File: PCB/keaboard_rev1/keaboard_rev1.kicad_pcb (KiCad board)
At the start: 2 copper layers, 141.9 x 93.7 mm, 61 parts, among them K01 KEYSW, K02 KEYSW, K03 KEYSW, K04 KEYSW, K05 KEYSW, K06 KEYSW, K07 KEYSW, K08 KEYSW, K09 KEYSW, K10 KEYSW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

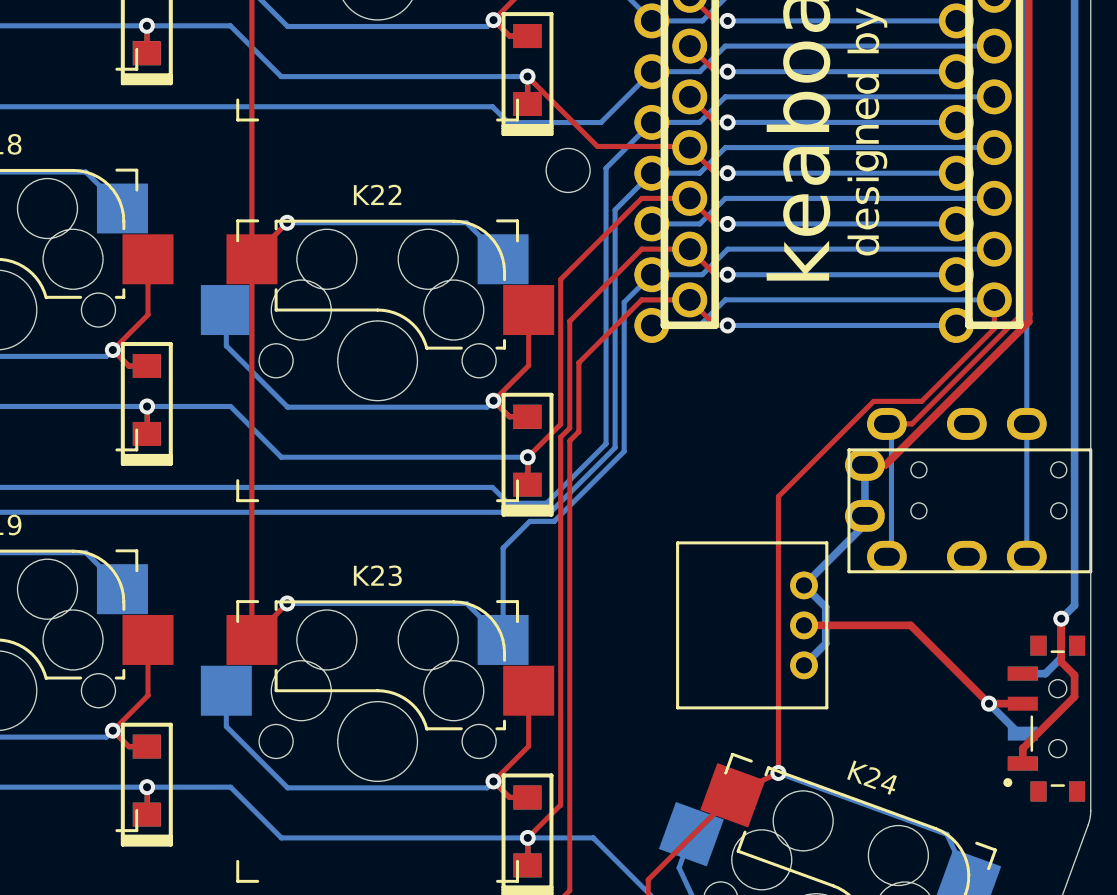
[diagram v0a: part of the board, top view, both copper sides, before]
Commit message: Fix missing trace
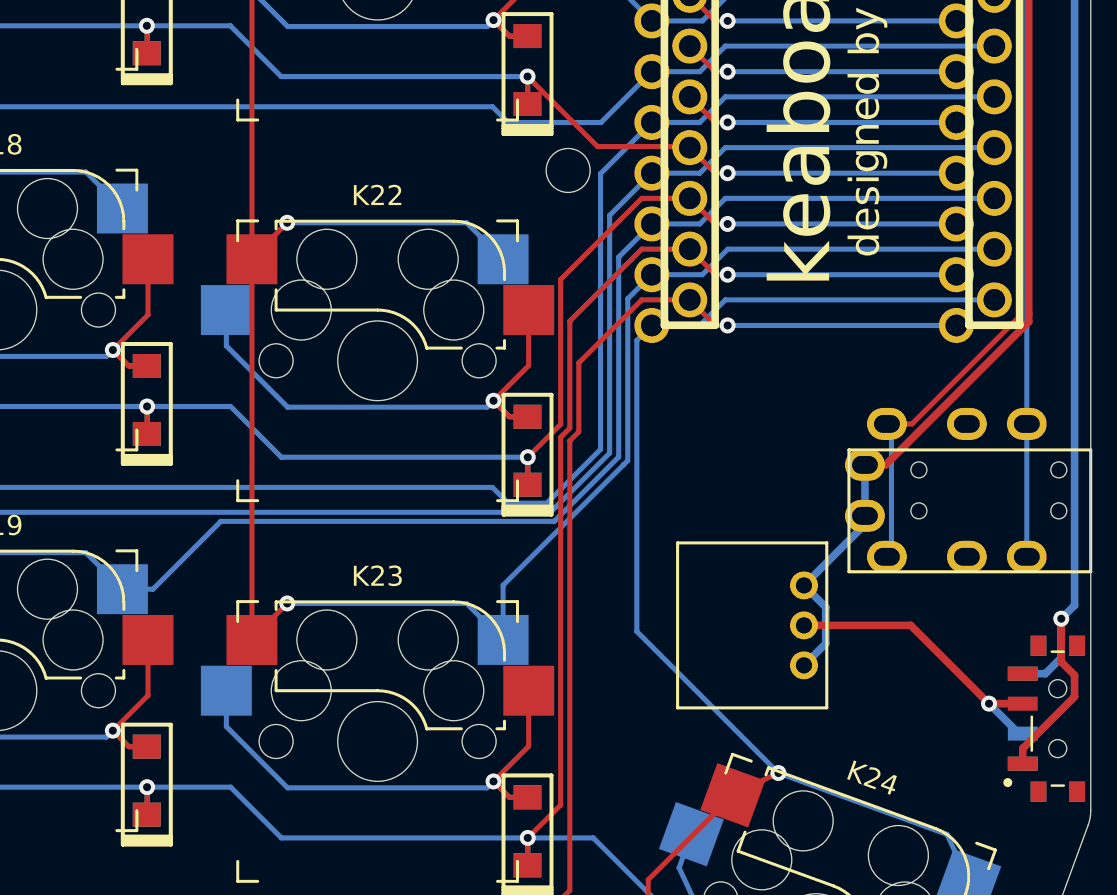
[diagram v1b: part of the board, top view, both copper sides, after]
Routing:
- net COL5: track 137.1 -> 177.0 mm
- net COL7: track 94.0 -> 90.1 mm
- net COL6: track 120.2 -> 119.5 mm

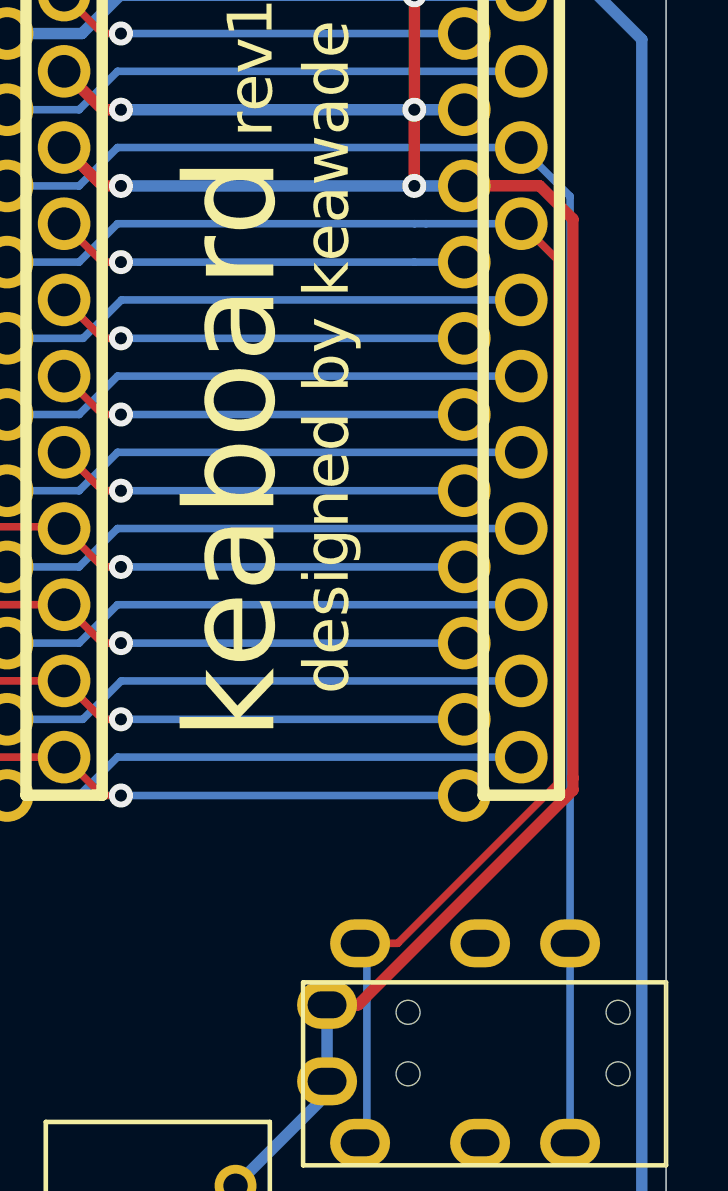
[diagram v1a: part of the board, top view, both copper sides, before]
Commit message: Update PCB to fix incorrect trace
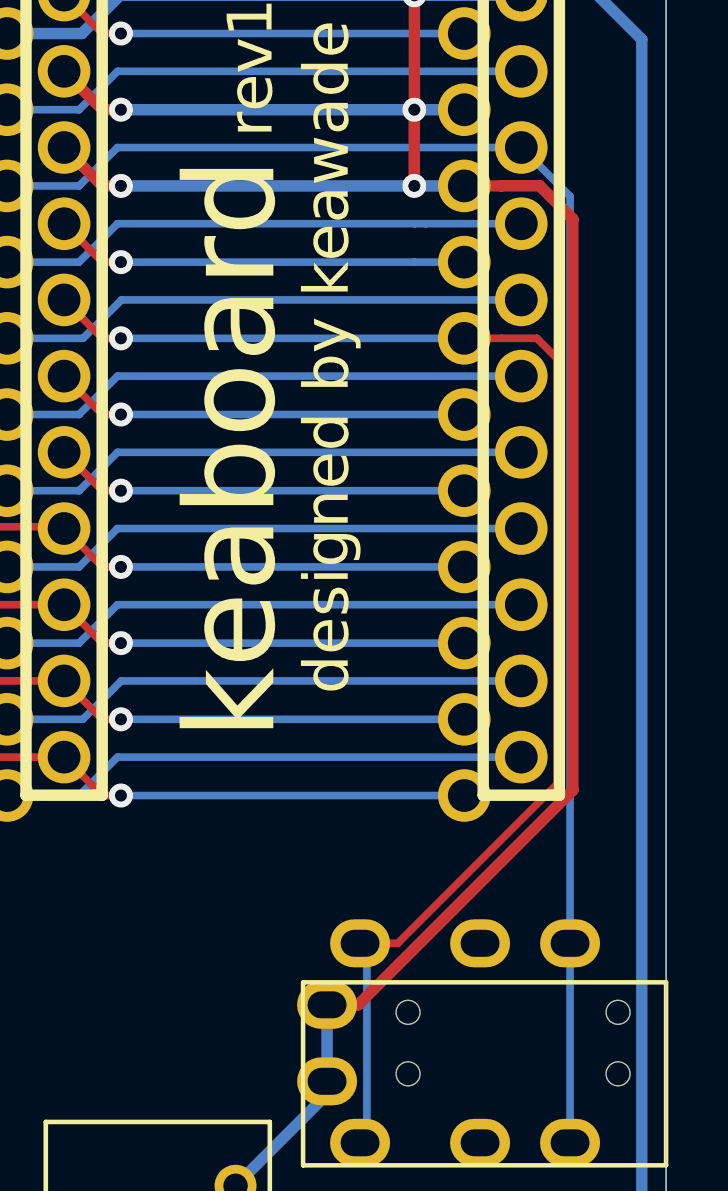
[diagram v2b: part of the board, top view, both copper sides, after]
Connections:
- U1 pad 20: SOFT_SERIAL_PIN -> Net-(U1-Pad20)
- U1 pad 6: Net-(U1-Pad6) -> SOFT_SERIAL_PIN
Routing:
- net Net-(U1-Pad20): track 0.00 -> 17.7 mm
- net Net-(U1-Pad6): track 13.9 -> 0.00 mm, vias 1 -> 0
- net SOFT_SERIAL_PIN: track 52.5 -> 47.0 mm, vias 0 -> 1

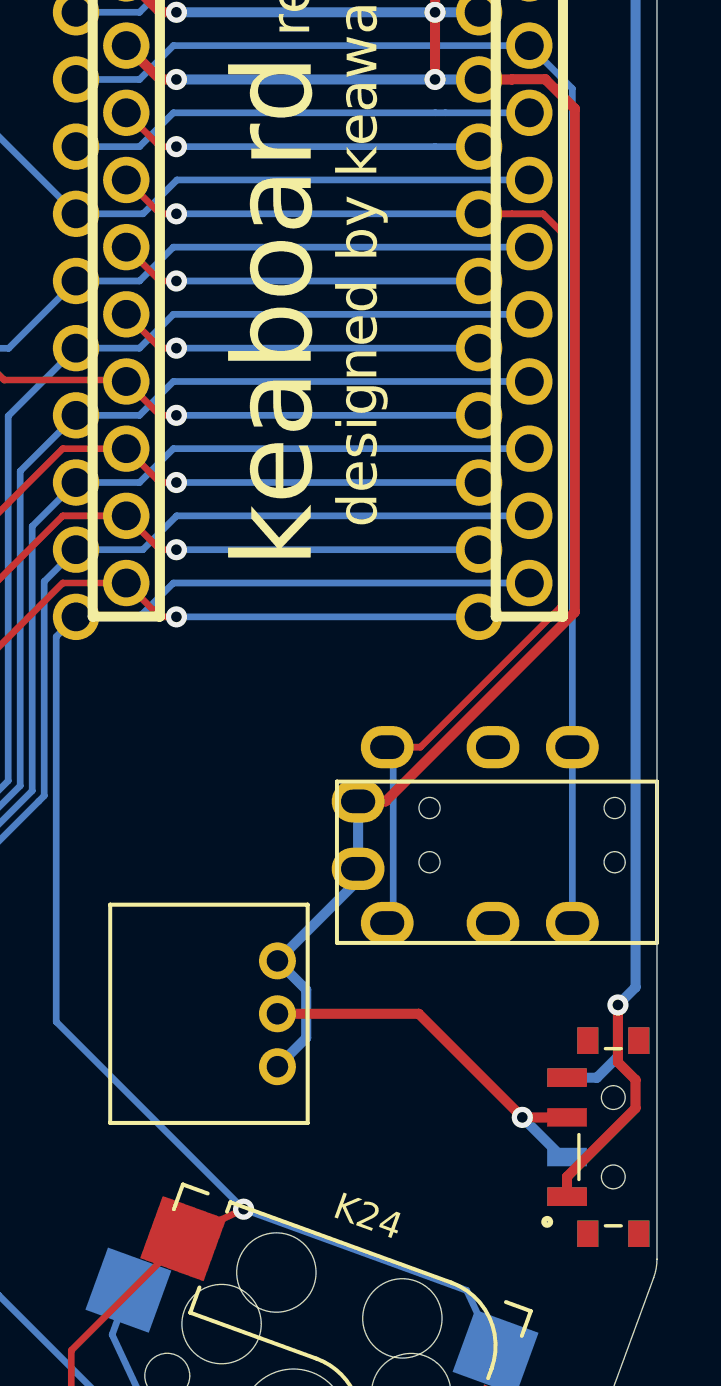
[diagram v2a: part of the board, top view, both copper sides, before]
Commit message: Improve labeling
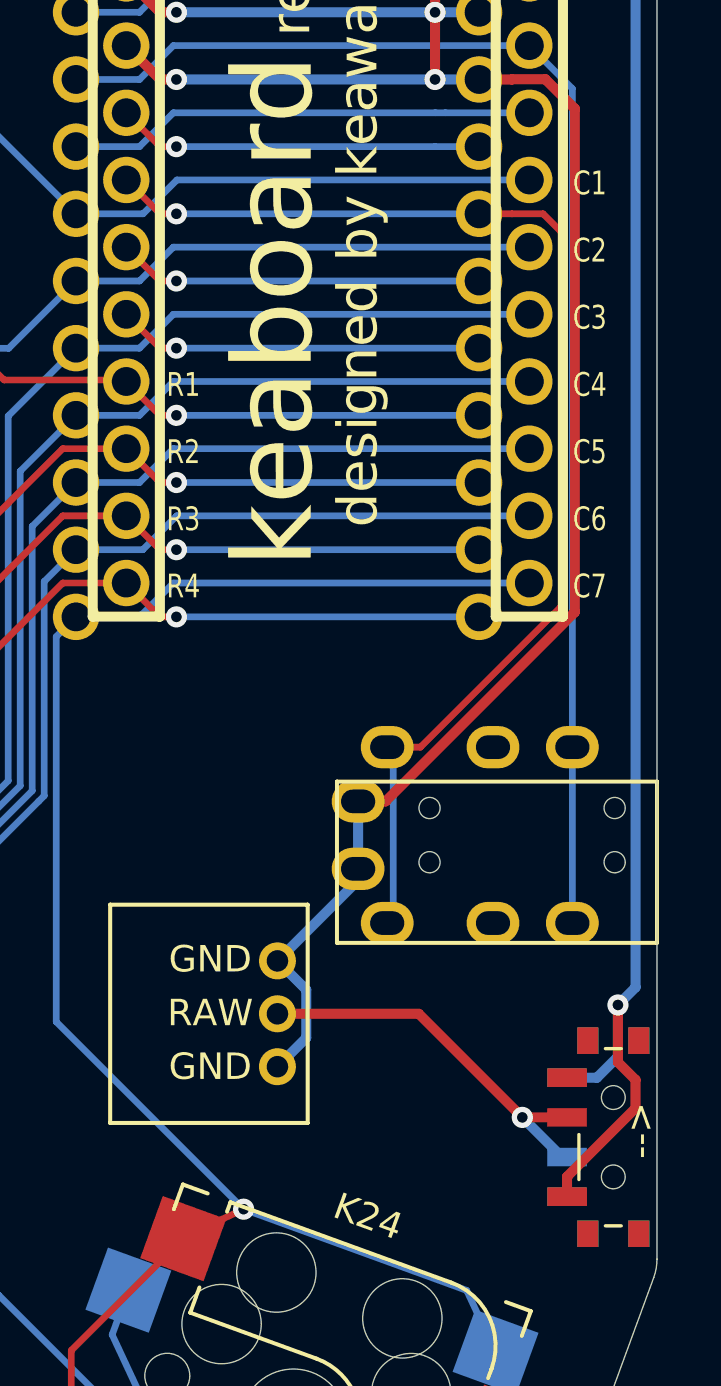
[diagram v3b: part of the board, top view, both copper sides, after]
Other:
- board text added: "C1"
- board text added: "C2"
- board text added: "C3"
- board text added: "C4"
- board text added: "C5"
- board text added: "C6"
- board text added: "C7"
- board text added: "R1"
- board text added: "R2"
- board text added: "R3"
- board text added: "R4"
